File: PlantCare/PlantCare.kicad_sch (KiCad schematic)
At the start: 4 parts, among them U1 AMS1117-3.3

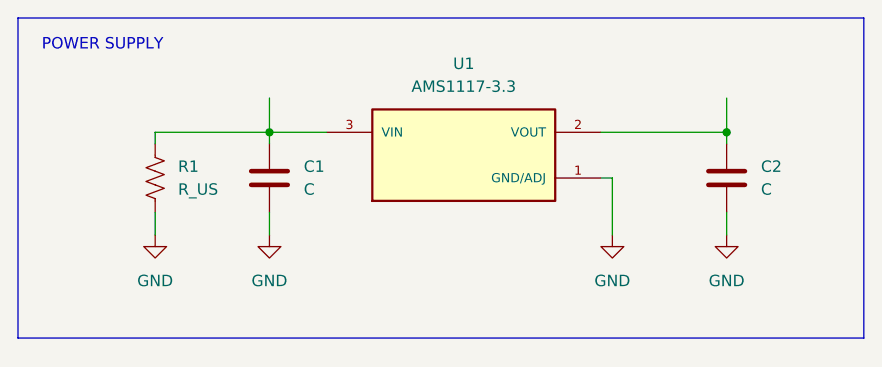
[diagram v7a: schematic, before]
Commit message: Add components specifications
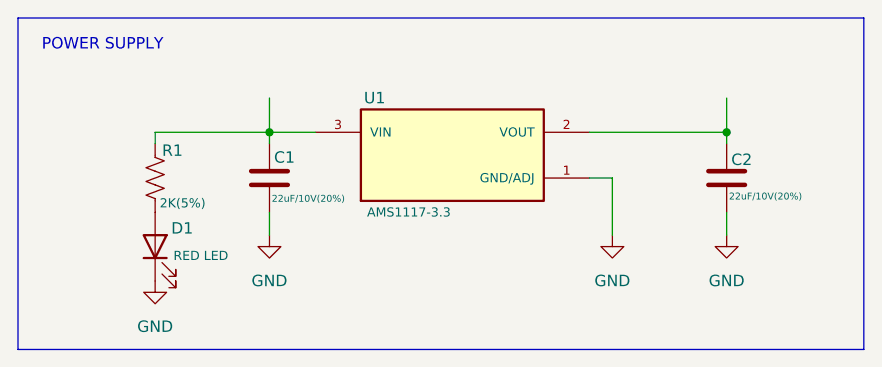
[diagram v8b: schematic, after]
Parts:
- added D1: RED LED, symbol Device:LED
- C1, C2: value C -> 22uF/10V(20%)
- R1: value R_US -> 2K(5%)
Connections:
- net GND: now also D1.1 (K); no longer R1.2
- new net: D1.2 (A), R1.2
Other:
- moved on the sheet: U1
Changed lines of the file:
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@@
 	(wire
 		(pts
-			(xy 87.63 38.1) (xy 101.6 38.1)
+			(xy 86.36 38.1) (xy 101.6 38.1)
 		)
 		(stroke
@@
 	(wire
 		(pts
-			(xy 87.63 43.18) (xy 88.9 43.18)
+			(xy 86.36 43.18) (xy 88.9 43.18)
 		)
 		(stroke
@@
 	(wire
 		(pts
-			(xy 38.1 46.99) (xy 38.1 49.53)
+			(xy 88.9 43.18) (xy 88.9 49.53)
 		)
 		(stroke
@@
 	(wire
 		(pts
-			(xy 88.9 43.18) (xy 88.9 49.53)
-		)
-		(stroke
-			(width 0)
-			(type default)
-		)
-	)
-	(wire
-		(pts
-			(xy 57.15 38.1) (xy 50.8 38.1)
+			(xy 55.88 38.1) (xy 50.8 38.1)
 		)
 		(stroke
@@
 	(rectangle
 		(start 22.86 25.4)
-		(end 116.84 60.96)
+		(end 116.84 62.23)
 		(stroke
 			(width 0)
@@
 		(shape round)
 		(at 50.8 34.29 0)
-		(fields_autoplaced yes)
 		(effects
 			(font
@@
 		)
 		(property "Netclass" "EXT_5V"
-			(at 51.4985 31.75 0)
+			(at 48.26 29.972 0)
 			(effects
 				(font
@@
 		(shape round)
 		(at 101.6 34.29 0)
-		(fields_autoplaced yes)
 		(effects
 			(font
@@
 		)
 		(property "Netclass" "VDD33"
-			(at 102.2985 31.75 0)
+			(at 98.552 29.972 0)
 			(effects
 				(font
@@
 		(on_board yes)
 		(dnp no)
-		(fields_autoplaced yes)
 		(property "Reference" "C2"
-			(at 105.41 41.9099 0)
+			(at 102.108 41.148 0)
 			(effects
 				(font
@@
 			)
 		)
-		(property "Value" "C"
-			(at 105.41 44.4499 0)
-			(effects
-				(font
-					(size 1.27 1.27)
+		(property "Value" "22uF/10V(20%)"
+			(at 101.854 45.212 0)
+			(effects
+				(font
+					(size 0.762 0.762)
 				)
 				(justify left)
@@
 		(on_board yes)
 		(dnp no)
-		(fields_autoplaced yes)
 		(property "Reference" "R1"
-			(at 40.64 41.9099 0)
+			(at 38.862 40.132 0)
 			(effects
 				(font
@@
 			)
 		)
-		(property "Value" "R_US"
-			(at 40.64 44.4499 0)
-			(effects
-				(font
-					(size 1.27 1.27)
+		(property "Value" "2K(5%)"
+			(at 38.608 45.974 0)
+			(effects
+				(font
+					(size 1.016 1.016)
 				)
 				(justify left)
@@
 	(symbol
 		(lib_id "AMS1117-3.3:AMS1117-3.3")
-		(at 72.39 40.64 0)
+		(at 71.12 40.64 0)
 		(unit 1)
 		(exclude_from_sim no)
@@
 		(on_board yes)
 		(dnp no)
-		(fields_autoplaced yes)
 		(property "Reference" "U1"
-			(at 72.39 30.48 0)
+			(at 62.484 34.29 0)
 			(effects
 				(font
@@
 		)
 		(property "Value" "AMS1117-3.3"
-			(at 72.39 33.02 0)
-			(effects
-				(font
-					(size 1.27 1.27)
+			(at 66.294 46.99 0)
+			(effects
+				(font
+					(size 1.016 1.016)
 				)
 			)
 		)
 		(property "Footprint" "SOT229P700X180-4N"
-			(at 72.39 40.64 0)
+			(at 71.12 40.64 0)
 			(effects
 				(font
@@
 		)
 		(property "Datasheet" ""
-			(at 72.39 40.64 0)
+			(at 71.12 40.64 0)
 			(effects
 				(font
@@
 		)
 		(property "Description" ""
-			(at 72.39 40.64 0)
+			(at 71.12 40.64 0)
 			(effects
 				(font
@@
 		)
 		(property "MF" "Advanced Monolithic Systems"
-			(at 72.39 40.64 0)
+			(at 71.12 40.64 0)
 			(effects
 				(font
@@
 		)
 		(property "MAXIMUM_PACKAGE_HEIGHT" "1.8 mm"
-			(at 72.39 40.64 0)
+			(at 71.12 40.64 0)
 			(effects
 				(font
@@
 		)
 		(property "Package" "SOT-223 Seeed Technology"
-			(at 72.39 40.64 0)
+			(at 71.12 40.64 0)
 			(effects
 				(font
@@
 		)
 		(property "Price" "None"
-			(at 72.39 40.64 0)
+			(at 71.12 40.64 0)
 			(effects
 				(font
@@
 		)
 		(property "Check_prices" "https://www.snapeda.com/parts/AMS1117-3.3/Advanced+Monolithic+Systems/view-part/?ref=eda"
-			(at 72.39 40.64 0)
+			(at 71.12 40.64 0)
 			(effects
 				(font
@@
 		)
 		(property "STANDARD" "IPC 7351B"
-			(at 72.39 40.64 0)
+			(at 71.12 40.64 0)
 			(effects
 				(font
@@
 		)
 		(property "PARTREV" "N/A"
-			(at 72.39 40.64 0)
+			(at 71.12 40.64 0)
 			(effects
 				(font
@@
 		)
 		(property "SnapEDA_Link" "https://www.snapeda.com/parts/AMS1117-3.3/Advanced+Monolithic+Systems/view-part/?ref=snap"
-			(at 72.39 40.64 0)
+			(at 71.12 40.64 0)
 			(effects
 				(font
@@
 		)
 		(property "SNAPEDA_PACKAGE_ID" "71280"
-			(at 72.39 40.64 0)
+			(at 71.12 40.64 0)
 			(effects
 				(font
@@
 		)
 		(property "MP" "AMS1117-3.3"
-			(at 72.39 40.64 0)
+			(at 71.12 40.64 0)
 			(effects
 				(font
@@
 		)
 		(property "Description_1" "\\nSot223/Pkg 1-Amp 3.3-Volt Low Drop Out Voltage Regulatator\\n"
-			(at 72.39 40.64 0)
+			(at 71.12 40.64 0)
 			(effects
 				(font
@@
 		)
 		(property "MANUFACTURER" "Advanced Monolithic Systems"
-			(at 72.39 40.64 0)
+			(at 71.12 40.64 0)
 			(effects
 				(font
@@
 		)
 		(property "Availability" "Not in stock"
-			(at 72.39 40.64 0)
+			(at 71.12 40.64 0)
 			(effects
 				(font
@@
 		)
 		(property "SNAPEDA_PN" "AMS1117-3.3"
-			(at 72.39 40.64 0)
+			(at 71.12 40.64 0)
 			(effects
 				(font
@@
 	(symbol
 		(lib_id "power:GND")
-		(at 38.1 49.53 0)
+		(at 38.1 54.61 0)
 		(unit 1)
 		(exclude_from_sim no)
@@
 		(fields_autoplaced yes)
 		(property "Reference" "#PWR01"
-			(at 38.1 55.88 0)
+			(at 38.1 60.96 0)
 			(effects
 				(font
@@
 		)
 		(property "Value" "GND"
+			(at 38.1 59.69 0)
+			(effects
+				(font
+					(size 1.27 1.27)
+				)
+			)
+		)
+		(property "Footprint" ""
 			(at 38.1 54.61 0)
 			(effects
@@
 					(size 1.27 1.27)
 				)
-			)
-		)
-		(property "Footprint" ""
-			(at 38.1 49.53 0)
-			(effects
-				(font
-					(size 1.27 1.27)
-				)
 				(hide yes)
 			)
 		)
 		(property "Datasheet" ""
-			(at 38.1 49.53 0)
+			(at 38.1 54.61 0)
 			(effects
 				(font
@@
 		)
 		(property "Description" "Power symbol creates a global label with name \"GND\" , ground"
-			(at 38.1 49.53 0)
+			(at 38.1 54.61 0)
 			(effects
 				(font
@@
 	)
 	(symbol
+		(lib_id "Device:LED")
+		(at 38.1 50.8 90)
+		(unit 1)
+		(exclude_from_sim no)
+		(in_bom yes)
+		(on_board yes)
+		(dnp no)
+		(property "Reference" "D1"
+			(at 39.878 48.768 90)
+			(effects
+				(font
+					(size 1.27 1.27)
+				)
+				(justify right)
+			)
+		)
+		(property "Value" "RED LED"
+			(at 40.132 51.816 90)
+			(effects
+				(font
+					(size 1.016 1.016)
+				)
+				(justify right)
+			)
+		)
+		(property "Footprint" ""
+			(at 38.1 50.8 0)
+			(effects
+				(font
+					(size 1.27 1.27)
+				)
+				(hide yes)
+			)
+		)
+		(property "Datasheet" "~"
+			(at 38.1 50.8 0)
+			(effects
+				(font
+					(size 1.27 1.27)
+				)
+				(hide yes)
+			)
+		)
+		(property "Description" "Light emitting diode"
+			(at 38.1 50.8 0)
+			(effects
+				(font
+					(size 1.27 1.27)
+				)
+				(hide yes)
+			)
+		)
+		(pin "1"
+		)
+		(pin "2"
+		)
+		(instances
+			(project ""
+				(path "/8b30f815-a35a-4dbb-8ef1-0ef116f0462d"
+					(reference "D1")
+					(unit 1)
+				)
+			)
+		)
+	)
+	(symbol
 		(lib_id "Device:C")
 		(at 50.8 43.18 0)
@@
 		(on_board yes)
 		(dnp no)
-		(fields_autoplaced yes)
 		(property "Reference" "C1"
-			(at 54.61 41.9099 0)
+			(at 51.308 40.894 0)
 			(effects
 				(font
@@
 			)
 		)
-		(property "Value" "C"
-			(at 54.61 44.4499 0)
-			(effects
-				(font
-					(size 1.27 1.27)
+		(property "Value" "22uF/10V(20%)"
+			(at 51.054 45.466 0)
+			(effects
+				(font
+					(size 0.762 0.762)
 				)
 				(justify left)
